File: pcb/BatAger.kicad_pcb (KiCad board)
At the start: 2 copper layers, 285.8 x 74.9 mm, 172 parts, among them CON1 AVR-ISP-6, IC1 ATMEGA2560-A, P1 FTDI, P10 CONN_01X02, P11 CONN_01X02, P12 CONN_01X02, P13 -15V, P14 GND, P15 AUX, P16 FAN, P2 +15V, P3 BAT1_TP, P4 BAT3_TP, P5 BAT5_TP, P6 BAT2_TP, P7 BAT4_TP, P8 CONN_01X02, P9 CONN_01X02, Q1 IRFR3607PBF, Q10 BC849, Q11 IRF9530, Q12 BC849, Q13 CSD18536KCS, Q14 BC849, Q15 IRF9530, Q16 BC849, Q17 CSD18536KCS, Q18 BC849, Q19 IRF9530, Q2 BC849, Q20 BC849, Q21 CSD18536KCS, Q22 IRFR3607PBF, Q23 BC849, Q24 BC849, Q3 IRF9530, Q4 CSD18536KCS, Q5 BC849, Q6 BC849, Q7 IRF9530, Q8 CSD18536KCS, Q9 BC849, SW1 SW_PUSH_4PIN, U1 MC33269, U2 LM358DUAL, U3 LM358DUAL, U4 LM358DUAL, U5 LM358DUAL, U6 LM358DUAL, Y1 16MHz

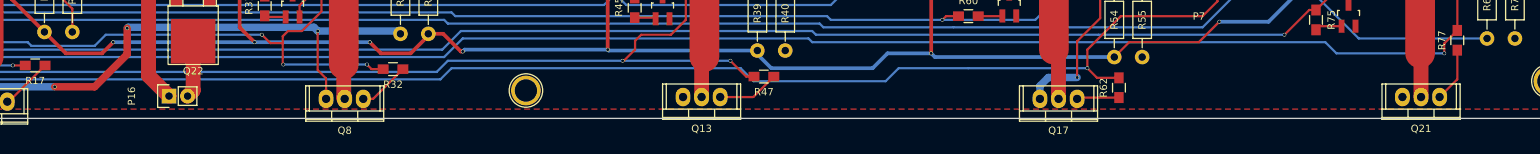
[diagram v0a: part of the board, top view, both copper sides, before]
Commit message: Added caps on discharge fet gates
Need to filter the digital signal from the MCU to create an analog
voltage at the gate because the fet should operate in between on and
off states (which generates heat due to high Rds).
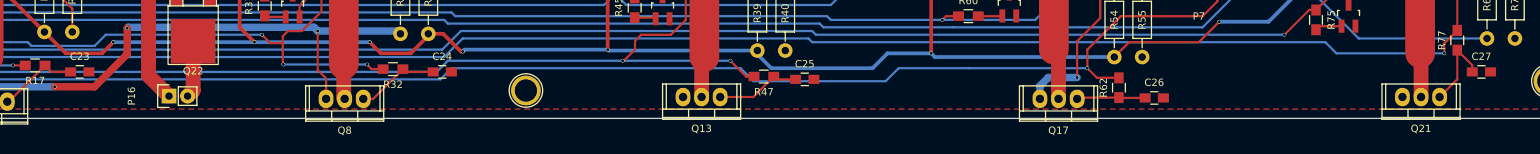
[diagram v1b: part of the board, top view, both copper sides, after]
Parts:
- added C23: 0.1uF, Capacitors_SMD:C_0805_HandSoldering, F.Cu at (91.4, 91.4)
- added C24: 0.1uF, Capacitors_SMD:C_0805_HandSoldering, F.Cu at (141.0, 91.4)
- added C25: 0.1uF, Capacitors_SMD:C_0805_HandSoldering, F.Cu at (190.5, 92.5)
- added C26: 0.1uF, Capacitors_SMD:C_0805_HandSoldering, F.Cu at (238.3, 95.0)
- added C27: 0.1uF, Capacitors_SMD:C_0805_HandSoldering, F.Cu at (283.0, 91.4)
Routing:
- net Net-(C24-Pad1): track 7.10 -> 11.4 mm
- net Net-(C23-Pad1): track 7.21 -> 11.1 mm
- net Net-(C27-Pad1): track 7.40 -> 11.2 mm
- net Net-(C26-Pad1): track 5.79 -> 9.38 mm
- net Net-(C25-Pad1): track 8.48 -> 11.6 mm

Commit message: Changed R62 & C26 to PTH.
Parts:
- C26: footprint Capacitors_SMD:C_0805_HandSoldering -> Capacitors_ThroughHole:C_Disc_D3_P2.5
- R62: footprint Resistors_SMD:R_0805_HandSoldering -> Custom Footprints:Resistor_Horizontal_RM10mm
- moved C26 6.60 mm to (244.9, 95.0)
- moved R62 6.45 mm to (239.8, 92.5), turned to 180 degrees
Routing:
- net Net-(C26-Pad1): track 9.38 -> 20.0 mm
- net /Sheet561D4A90/dchg_ctrl4: track 256.4 -> 257.8 mm

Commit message: Minor package changes.
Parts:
- C23, C24, C25, C26, C27: value 0.1uF -> 1uF
- P10, P11, P12, P8, P9: footprint Pin_Headers:Pin_Header_Straight_1x02 -> Custom Footprints:PINHEAD1-2_200mil
- R17, R32, R47, R62, R77: value 200 -> 15k
- moved P10 2.69 mm to (179.1, 25.9), turned to 0 degrees
- moved P9 2.69 mm to (130.3, 26.2), turned to 0 degrees
- moved P8 2.65 mm to (81.5, 26.2), turned to 0 degrees
- moved P12 2.65 mm to (277.1, 25.9), turned to 0 degrees
- moved P11 2.50 mm to (227.6, 25.9), turned to 0 degrees
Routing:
- net /Sheet561CB83A/bat1+: track 22.9 -> 23.7 mm
- net /Sheet561DD110/bat5+: track 22.9 -> 23.7 mm
- net /Sheet561D4A90/bat4+: track 23.0 -> 23.7 mm
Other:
- board text added: "CC1"
- board text added: "D14"
- board text added: "D15"
- board text added: "D16"
- board text added: "D17"
- board text added: "D18"
- board text added: "D19"
- board text added: "DCC1"
- board text added: "DCLED1"
- board text added: "GND"
- board text added: "I1"
- board text added: "VBAT1"
